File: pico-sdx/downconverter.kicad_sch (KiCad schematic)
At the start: 33 parts, among them T1 T-622, U1 74HC74, U2 4066, U3 OPA2350

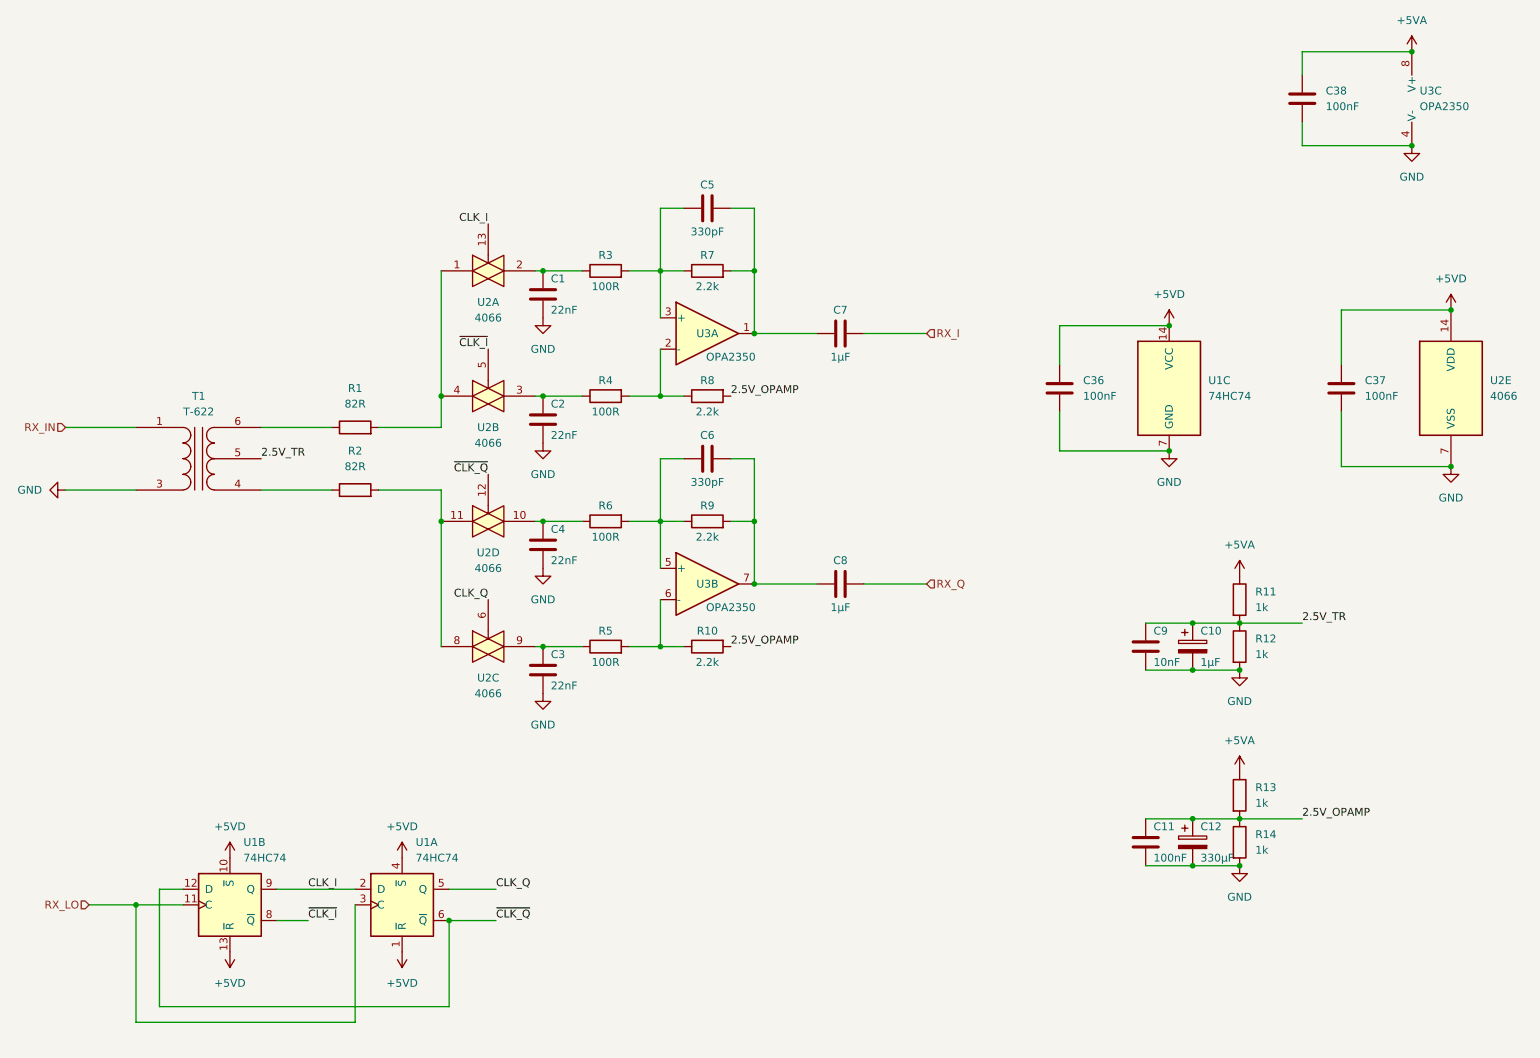
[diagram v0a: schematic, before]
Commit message: add documentation and RaspberryPi Pico
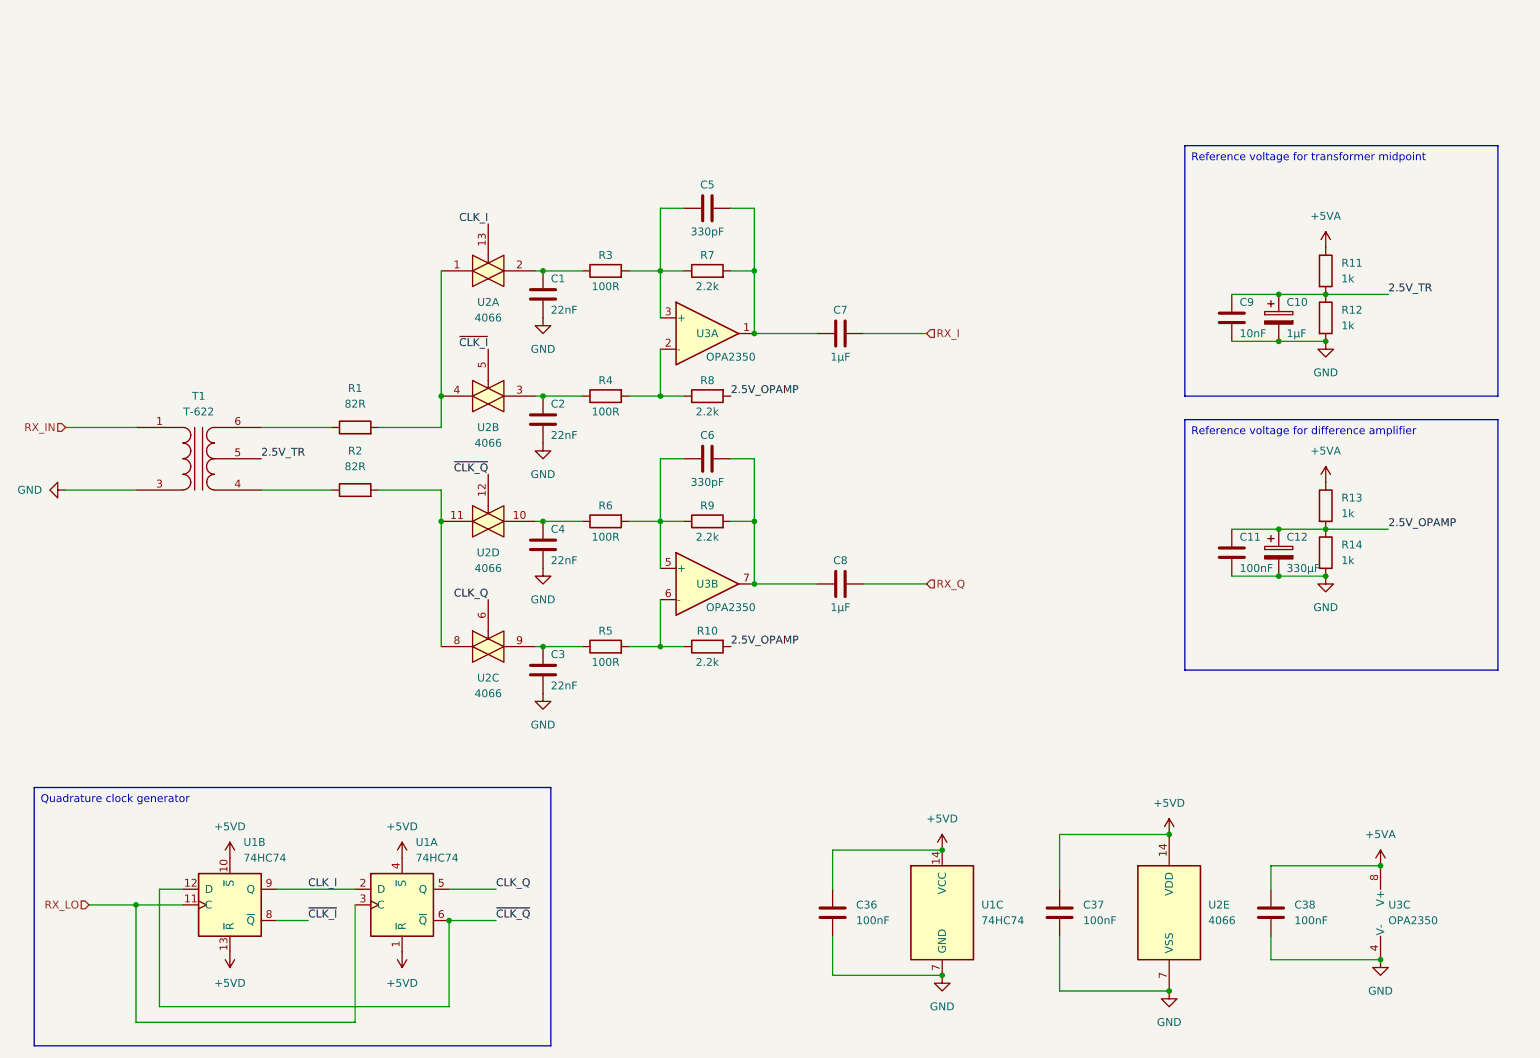
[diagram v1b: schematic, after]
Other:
- moved on the sheet: C10, C11, C12, C36, C37, C38, C9, R11, R12, R13, R14, U1C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

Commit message: routed with filter relays without PA
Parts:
- added TP3: RX_TR_Midpoint, TestPoint:TestPoint_Loop_D1.80mm_Drill1.0mm_Beaded, symbol Connector:TestPoint
- added TP4: RX_OPAMP_Midpoint, TestPoint:TestPoint_Loop_D1.80mm_Drill1.0mm_Beaded, symbol Connector:TestPoint
- renumbered C4 to C10, C3 to C11, C5 to C12, C6 to C13, C36 to C14, C7 to C15, C8 to C16, C37 to C17, C9 to C18, C11 to C19, C38 to C20, C10 to C21, C12 to C22, C1 to C8, C2 to C9, R6 to R5, R5 to R6, U1 to U6, U2 to U7, U3 to U8
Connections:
- net 2.5V_OPAMP: now also TP4.1
- net 2.5V_TR: now also TP3.1

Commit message: modular design
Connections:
- net +5VD renamed +3.3V
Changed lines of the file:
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@@
 	)
 	(symbol
-		(lib_id "power:+5VD")
+		(lib_id "power:+3.3V")
 		(at 93.98 130.81 0)
 		(unit 1)
@@
 			)
 		)
-		(property "Value" "+5VD"
+		(property "Value" "+3.3V"
 			(at 93.98 125.73 0)
 			(effects
@@
 			)
 		)
-		(property "Description" "Power symbol creates a global label with name \"+5VD\""
+		(property "Description" "Power symbol creates a global label with name \"+3.3V\""
 			(at 93.98 130.81 0)
 			(effects
@@
 	)
 	(symbol
-		(lib_id "power:+5VD")
+		(lib_id "power:+3.3V")
 		(at 218.44 127 0)
 		(unit 1)
@@
 			)
 		)
-		(property "Value" "+5VD"
+		(property "Value" "+3.3V"
 			(at 218.44 121.92 0)
 			(effects
@@
 			)
 		)
-		(property "Description" "Power symbol creates a global label with name \"+5VD\""
+		(property "Description" "Power symbol creates a global label with name \"+3.3V\""
 			(at 218.44 127 0)
 			(effects
@@
 	)
 	(symbol
-		(lib_id "power:+5VD")
+		(lib_id "power:+3.3V")
 		(at 66.04 130.81 0)
 		(unit 1)
@@
 			)
 		)
-		(property "Value" "+5VD"
+		(property "Value" "+3.3V"
 			(at 66.04 125.73 0)
 			(effects
@@
 			)
 		)
-		(property "Description" "Power symbol creates a global label with name \"+5VD\""
+		(property "Description" "Power symbol creates a global label with name \"+3.3V\""
 			(at 66.04 130.81 0)
 			(effects
@@
 	)
 	(symbol
-		(lib_id "power:+5VD")
+		(lib_id "power:+3.3V")
 		(at 181.61 129.54 0)
 		(unit 1)
@@
 			)
 		)
-		(property "Value" "+5VD"
+		(property "Value" "+3.3V"
 			(at 181.61 124.46 0)
 			(effects
@@
 			)
 		)
-		(property "Description" "Power symbol creates a global label with name \"+5VD\""
+		(property "Description" "Power symbol creates a global label with name \"+3.3V\""
 			(at 181.61 129.54 0)
 			(effects
@@
 	)
 	(symbol
-		(lib_id "power:+5VD")
+		(lib_id "power:+3.3V")
 		(at 66.04 146.05 180)
 		(unit 1)
@@
 			)
 		)
-		(property "Value" "+5VD"
+		(property "Value" "+3.3V"
 			(at 66.04 151.13 0)
 			(effects
@@
 			)
 		)
-		(property "Description" "Power symbol creates a global label with name \"+5VD\""
+		(property "Description" "Power symbol creates a global label with name \"+3.3V\""
 			(at 66.04 146.05 0)
 			(effects
@@
 	)
 	(symbol
-		(lib_id "power:+5VD")
+		(lib_id "power:+3.3V")
 		(at 93.98 146.05 180)
 		(unit 1)
@@
 			)
 		)
-		(property "Value" "+5VD"
+		(property "Value" "+3.3V"
 			(at 93.98 151.13 0)
 			(effects
@@
 			)
 		)
-		(property "Description" "Power symbol creates a global label with name \"+5VD\""
+		(property "Description" "Power symbol creates a global label with name \"+3.3V\""
 			(at 93.98 146.05 0)
 			(effects

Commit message: mixer routed
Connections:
- net CLK_I: now also U6.12 (D), U6.5 (Q); no longer U6.2 (D), U6.9 (Q)
- net CLK_Q: now also U6.9 (Q); no longer U6.5 (Q)
- net ~{CLK_I}: now also U6.6 (~{Q}); no longer U6.8 (~{Q})
- net ~{CLK_Q}: now also U6.2 (D), U6.8 (~{Q}); no longer U6.12 (D), U6.6 (~{Q})
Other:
- moved on the sheet: U6A, U6B
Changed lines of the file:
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@@
+	)
+	(junction
+		(at 135.89 35.56)
+		(diameter 0)
+		(color 0 0 0 0)
+	)
+	(junction
+		(at 151.13 86.36)
+		(diameter 0)
+		(color 0 0 0 0)
+	)
+	(junction
+		(at 135.89 76.2)
+		(diameter 0)
+		(color 0 0 0 0)
+	)
+	(junction
+		(at 236.22 39.37)
+		(diameter 0)
+		(color 0 0 0 0)
+	)
+	(junction
+		(at 243.84 85.09)
+		(diameter 0)
+		(color 0 0 0 0)
+	)
+	(junction
+		(at 116.84 35.56)
+		(diameter 0)
+		(color 0 0 0 0)
+	)
+	(junction
+		(at 236.22 85.09)
+		(diameter 0)
+		(color 0 0 0 0)
+	)
+	(junction
+		(at 218.44 127)
+		(diameter 0)
+		(color 0 0 0 0)
+	)
+	(junction
+		(at 252.73 147.32)
+		(diameter 0)
+		(color 0 0 0 0)
+	)
+	(junction
+		(at 218.44 152.4)
+		(diameter 0)
+		(color 0 0 0 0)
+	)
+	(junction
+		(at 100.33 76.2)
+		(diameter 0)
+		(color 0 0 0 0)
+	)
+	(junction
+		(at 243.84 39.37)
+		(diameter 0)
+		(color 0 0 0 0)
+	)
+	(junction
+		(at 135.89 55.88)
+		(diameter 0)
+		(color 0 0 0 0)
+	)
+	(junction
+		(at 151.13 76.2)
+		(diameter 0)
+		(color 0 0 0 0)
+	)
+	(junction
+		(at 151.13 35.56)
+		(diameter 0)
+		(color 0 0 0 0)
+	)
+	(junction
+		(at 251.46 77.47)
+		(diameter 0)
+		(color 0 0 0 0)
+	)
+	(junction
+		(at 181.61 129.54)
+		(diameter 0)
+		(color 0 0 0 0)
+	)
+	(junction
+		(at 50.8 138.43)
+		(diameter 0)
+		(color 0 0 0 0)
+	)
+	(junction
+		(at 116.84 96.52)
+		(diameter 0)
+		(color 0 0 0 0)
+	)
+	(junction
+		(at 151.13 45.72)
+		(diameter 0)
+		(color 0 0 0 0)
+	)
+	(junction
+		(at 116.84 76.2)
+		(diameter 0)
+		(color 0 0 0 0)
+	)
+	(junction
+		(at 116.84 55.88)
+		(diameter 0)
+		(color 0 0 0 0)
+	)
+	(junction
+		(at 236.22 77.47)
+		(diameter 0)
+		(color 0 0 0 0)
+	)
+	(junction
+		(at 252.73 132.08)
+		(diameter 0)
+		(color 0 0 0 0)
+	)
+	(junction
+		(at 135.89 96.52)
+		(diameter 0)
+		(color 0 0 0 0)
+	)
+	(junction
+		(at 100.33 55.88)
+		(diameter 0)
+		(color 0 0 0 0)
+	)
+	(junction
+		(at 251.46 39.37)
+		(diameter 0)
+		(color 0 0 0 0)
 	)
 	(junction
 		(at 101.6 140.97)
-		(diameter 0)
-		(color 0 0 0 0)
-	)
-	(junction
-		(at 135.89 35.56)
-		(diameter 0)
-		(color 0 0 0 0)
-	)
-	(junction
-		(at 151.13 86.36)
-		(diameter 0)
-		(color 0 0 0 0)
-	)
-	(junction
-		(at 135.89 76.2)
-		(diameter 0)
-		(color 0 0 0 0)
-	)
-	(junction
-		(at 236.22 39.37)
-		(diameter 0)
-		(color 0 0 0 0)
-	)
-	(junction
-		(at 243.84 85.09)
-		(diameter 0)
-		(color 0 0 0 0)
-	)
-	(junction
-		(at 116.84 35.56)
-		(diameter 0)
-		(color 0 0 0 0)
-	)
-	(junction
-		(at 236.22 85.09)
-		(diameter 0)
-		(color 0 0 0 0)
-	)
-	(junction
-		(at 218.44 127)
-		(diameter 0)
-		(color 0 0 0 0)
-	)
-	(junction
-		(at 252.73 147.32)
-		(diameter 0)
-		(color 0 0 0 0)
-	)
-	(junction
-		(at 218.44 152.4)
-		(diameter 0)
-		(color 0 0 0 0)
-	)
-	(junction
-		(at 100.33 76.2)
-		(diameter 0)
-		(color 0 0 0 0)
-	)
-	(junction
-		(at 243.84 39.37)
-		(diameter 0)
-		(color 0 0 0 0)
-	)
-	(junction
-		(at 135.89 55.88)
-		(diameter 0)
-		(color 0 0 0 0)
-	)
-	(junction
-		(at 151.13 76.2)
-		(diameter 0)
-		(color 0 0 0 0)
-	)
-	(junction
-		(at 151.13 35.56)
-		(diameter 0)
-		(color 0 0 0 0)
-	)
-	(junction
-		(at 251.46 77.47)
-		(diameter 0)
-		(color 0 0 0 0)
-	)
-	(junction
-		(at 181.61 129.54)
-		(diameter 0)
-		(color 0 0 0 0)
-	)
-	(junction
-		(at 50.8 138.43)
-		(diameter 0)
-		(color 0 0 0 0)
-	)
-	(junction
-		(at 116.84 96.52)
-		(diameter 0)
-		(color 0 0 0 0)
-	)
-	(junction
-		(at 151.13 45.72)
-		(diameter 0)
-		(color 0 0 0 0)
-	)
-	(junction
-		(at 116.84 76.2)
-		(diameter 0)
-		(color 0 0 0 0)
-	)
-	(junction
-		(at 116.84 55.88)
-		(diameter 0)
-		(color 0 0 0 0)
-	)
-	(junction
-		(at 236.22 77.47)
-		(diameter 0)
-		(color 0 0 0 0)
-	)
-	(junction
-		(at 252.73 132.08)
-		(diameter 0)
-		(color 0 0 0 0)
-	)
-	(junction
-		(at 135.89 96.52)
-		(diameter 0)
-		(color 0 0 0 0)
-	)
-	(junction
-		(at 100.33 55.88)
-		(diameter 0)
-		(color 0 0 0 0)
-	)
-	(junction
-		(at 251.46 39.37)
 		(diameter 0)
 		(color 0 0 0 0)
@@
 	(symbol
 		(lib_id "74xx:74HC74")
-		(at 93.98 138.43 0)
+		(at 66.04 138.43 0)
 		(unit 1)
 		(exclude_from_sim no)
@@
 		(fields_autoplaced yes)
 		(property "Reference" "U6"
-			(at 96.1741 128.27 0)
+			(at 68.2341 128.27 0)
 			(effects
 				(font
@@
 		)
 		(property "Value" "74HC74"
-			(at 96.1741 130.81 0)
+			(at 68.2341 130.81 0)
 			(effects
 				(font
@@
 		)
 		(property "Footprint" "Package_SO:SOIC-14_3.9x8.7mm_P1.27mm"
-			(at 93.98 138.43 0)
+			(at 66.04 138.43 0)
 			(effects
 				(font
@@
 		)
 		(property "Datasheet" "74xx/74hc_hct74.pdf"
-			(at 93.98 138.43 0)
+			(at 66.04 138.43 0)
 			(effects
 				(font
@@
 		)
 		(property "Description" "Dual D Flip-flop, Set & Reset"
-			(at 93.98 138.43 0)
+			(at 66.04 138.43 0)
 			(effects
 				(font
@@
 	(symbol
 		(lib_id "74xx:74HC74")
-		(at 66.04 138.43 0)
+		(at 93.98 138.43 0)
 		(unit 2)
 		(exclude_from_sim no)
@@
 		(fields_autoplaced yes)
 		(property "Reference" "U6"
-			(at 68.2341 128.27 0)
+			(at 96.1741 128.27 0)
 			(effects
 				(font
@@
 		)
 		(property "Value" "74HC74"
-			(at 68.2341 130.81 0)
+			(at 96.1741 130.81 0)
 			(effects
 				(font
@@
 		)
 		(property "Footprint" "Package_SO:SOIC-14_3.9x8.7mm_P1.27mm"
-			(at 66.04 138.43 0)
+			(at 93.98 138.43 0)
 			(effects
 				(font
@@
 		)
 		(property "Datasheet" "74xx/74hc_hct74.pdf"
-			(at 66.04 138.43 0)
+			(at 93.98 138.43 0)
 			(effects
 				(font
@@
 		)
 		(property "Description" "Dual D Flip-flop, Set & Reset"
-			(at 66.04 138.43 0)
-			(effects
-				(font
+			(at 93.98 138.43 0)
+			(effects
+				(font
